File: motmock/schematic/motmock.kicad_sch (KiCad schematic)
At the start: 13 parts, among them J1 5V_in, J2 GND_in, J3 triac_trig_in, J4 ISP, J5 50_Hz_out, J6 speedo_out, M1 Motor_DC, Q1 BD139, U1 ATmega8-16P

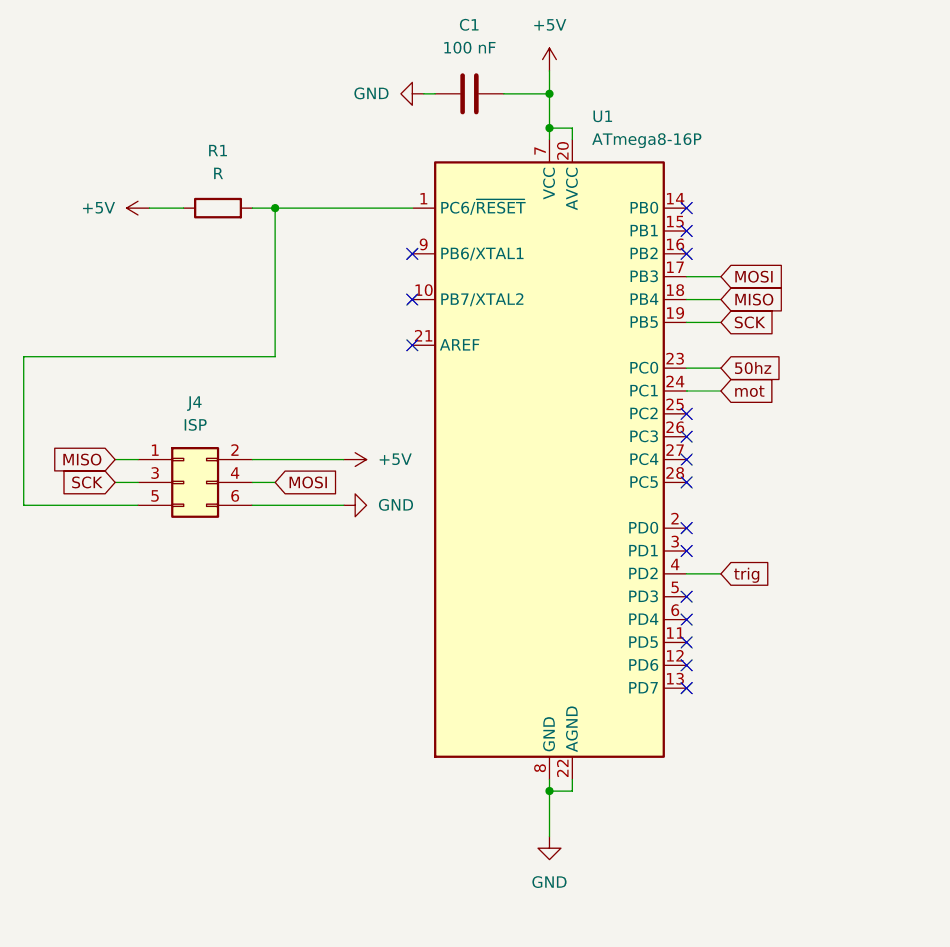
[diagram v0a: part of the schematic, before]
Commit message: Add motor mock base
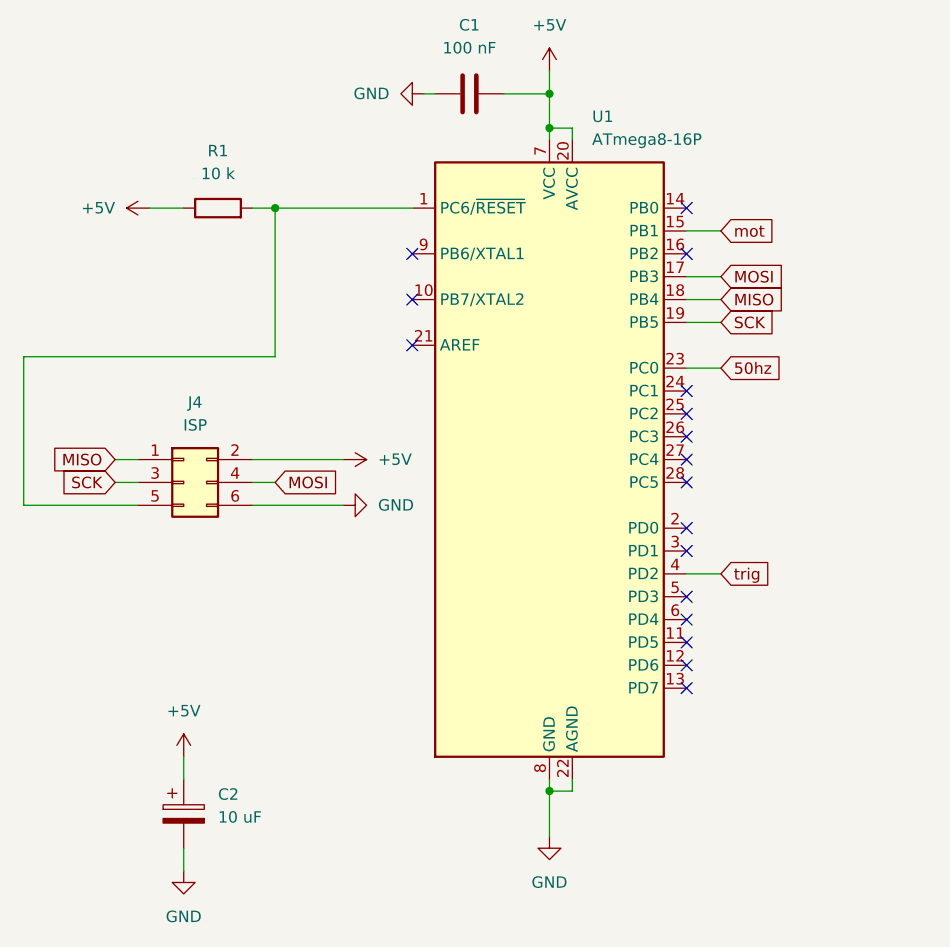
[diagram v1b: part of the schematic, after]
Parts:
- added C2: 10 uF, symbol Device:C_Polarized
- R1: value R -> 10 k
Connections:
- net +5V: now also C2.1
- net GND: now also C2.2
- net mot: now also U1.15 (PB1); no longer U1.24 (PC1)
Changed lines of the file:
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@@
-	)
-	(no_connect
-		(at 130.81 95.25)
 	)
 	(no_connect
@@
 		(at 130.81 143.51)
 	)
+	(no_connect
+		(at 130.81 113.03)
+	)
 	(wire
 		(pts
@@
 	(wire
 		(pts
+			(xy 74.93 163.83) (xy 74.93 166.37)
+		)
+		(stroke
+			(width 0)
+			(type default)
+		)
+	)
+	(wire
+		(pts
 			(xy 82.55 125.73) (xy 92.71 125.73)
 		)
@@
 	(wire
 		(pts
+			(xy 130.81 95.25) (xy 134.62 95.25)
+		)
+		(stroke
+			(width 0)
+			(type default)
+		)
+	)
+	(wire
+		(pts
 			(xy 35.56 38.1) (xy 41.91 38.1)
 		)
@@
 	(wire
 		(pts
+			(xy 74.93 153.67) (xy 74.93 156.21)
+		)
+		(stroke
+			(width 0)
+			(type default)
+		)
+	)
+	(wire
+		(pts
 			(xy 219.71 114.3) (xy 219.71 118.11)
 		)
@@
 		(pts
 			(xy 85.09 92.71) (xy 100.33 92.71)
-		)
-		(stroke
-			(width 0)
-			(type default)
-		)
-	)
-	(wire
-		(pts
-			(xy 130.81 113.03) (xy 134.62 113.03)
 		)
 		(stroke
@@
 	(global_label "mot"
 		(shape input)
-		(at 134.62 113.03 0)
+		(at 134.62 95.25 0)
 		(fields_autoplaced yes)
 		(effects
@@
 		)
 		(property "Intersheetrefs" "${INTERSHEET_REFS}"
-			(at 141.1732 113.03 0)
+			(at 141.1732 95.25 0)
 			(effects
 				(font
@@
 	)
 	(symbol
+		(lib_id "Device:C_Polarized")
+		(at 74.93 160.02 0)
+		(unit 1)
+		(exclude_from_sim no)
+		(in_bom yes)
+		(on_board yes)
+		(dnp no)
+		(fields_autoplaced yes)
+		(property "Reference" "C2"
+			(at 78.74 157.8609 0)
+			(effects
+				(font
+					(size 1.27 1.27)
+				)
+				(justify left)
+			)
+		)
+		(property "Value" "10 uF"
+			(at 78.74 160.4009 0)
+			(effects
+				(font
+					(size 1.27 1.27)
+				)
+				(justify left)
+			)
+		)
+		(property "Footprint" ""
+			(at 75.8952 163.83 0)
+			(effects
+				(font
+					(size 1.27 1.27)
+				)
+				(hide yes)
+			)
+		)
+		(property "Datasheet" "~"
+			(at 74.93 160.02 0)
+			(effects
+				(font
+					(size 1.27 1.27)
+				)
+				(hide yes)
+			)
+		)
+		(property "Description" "Polarized capacitor"
+			(at 74.93 160.02 0)
+			(effects
+				(font
+					(size 1.27 1.27)
+				)
+				(hide yes)
+			)
+		)
+		(pin "1"
+		)
+		(pin "2"
+		)
+		(instances
+			(project ""
+				(path "/0a4d76bd-d9dd-401a-acab-a3d06f37f9ef"
+					(reference "C2")
+					(unit 1)
+				)
+			)
+		)
+	)
+	(symbol
 		(lib_id "power:+5V")
 		(at 41.91 30.48 270)
@@
 	(symbol
 		(lib_id "power:GND")
+		(at 74.93 166.37 0)
+		(unit 1)
+		(exclude_from_sim no)
+		(in_bom yes)
+		(on_board yes)
+		(dnp no)
+		(fields_autoplaced yes)
+		(property "Reference" "#PWR013"
+			(at 74.93 172.72 0)
+			(effects
+				(font
+					(size 1.27 1.27)
+				)
+				(hide yes)
+			)
+		)
+		(property "Value" "GND"
+			(at 74.93 171.45 0)
+			(effects
+				(font
+					(size 1.27 1.27)
+				)
+			)
+		)
+		(property "Footprint" ""
+			(at 74.93 166.37 0)
+			(effects
+				(font
+					(size 1.27 1.27)
+				)
+				(hide yes)
+			)
+		)
+		(property "Datasheet" ""
+			(at 74.93 166.37 0)
+			(effects
+				(font
+					(size 1.27 1.27)
+				)
+				(hide yes)
+			)
+		)
+		(property "Description" "Power symbol creates a global label with name \"GND\" , ground"
+			(at 74.93 166.37 0)
+			(effects
+				(font
+					(size 1.27 1.27)
+				)
+				(hide yes)
+			)
+		)
+		(pin "1"
+		)
+		(instances
+			(project "motmock"
+				(path "/0a4d76bd-d9dd-401a-acab-a3d06f37f9ef"
+					(reference "#PWR013")
+					(unit 1)
+				)
+			)
+		)
+	)
+	(symbol
+		(lib_id "power:GND")
 		(at 101.6 80.01 270)
 		(unit 1)
@@
 	(symbol
 		(lib_id "power:+5V")
+		(at 74.93 153.67 0)
+		(unit 1)
+		(exclude_from_sim no)
+		(in_bom yes)
+		(on_board yes)
+		(dnp no)
+		(fields_autoplaced yes)
+		(property "Reference" "#PWR012"
+			(at 74.93 157.48 0)
+			(effects
+				(font
+					(size 1.27 1.27)
+				)
+				(hide yes)
+			)
+		)
+		(property "Value" "+5V"
+			(at 74.93 148.59 0)
+			(effects
+				(font
+					(size 1.27 1.27)
+				)
+			)
+		)
+		(property "Footprint" ""
+			(at 74.93 153.67 0)
+			(effects
+				(font
+					(size 1.27 1.27)
+				)
+				(hide yes)
+			)
+		)
+		(property "Datasheet" ""
+			(at 74.93 153.67 0)
+			(effects
+				(font
+					(size 1.27 1.27)
+				)
+				(hide yes)
+			)
+		)
+		(property "Description" "Power symbol creates a global label with name \"+5V\""
+			(at 74.93 153.67 0)
+			(effects
+				(font
+					(size 1.27 1.27)
+				)
+				(hide yes)
+			)
+		)
+		(pin "1"
+		)
+		(instances
+			(project "motmock"
+				(path "/0a4d76bd-d9dd-401a-acab-a3d06f37f9ef"
+					(reference "#PWR012")
+					(unit 1)
+				)
+			)
+		)
+	)
+	(symbol
+		(lib_id "power:+5V")
 		(at 71.12 92.71 90)
 		(unit 1)
@@
 			)
 		)
-		(property "Value" "R"
+		(property "Value" "10 k"
 			(at 78.74 88.9 90)
 			(effects
